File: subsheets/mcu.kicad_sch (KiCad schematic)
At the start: 4 parts

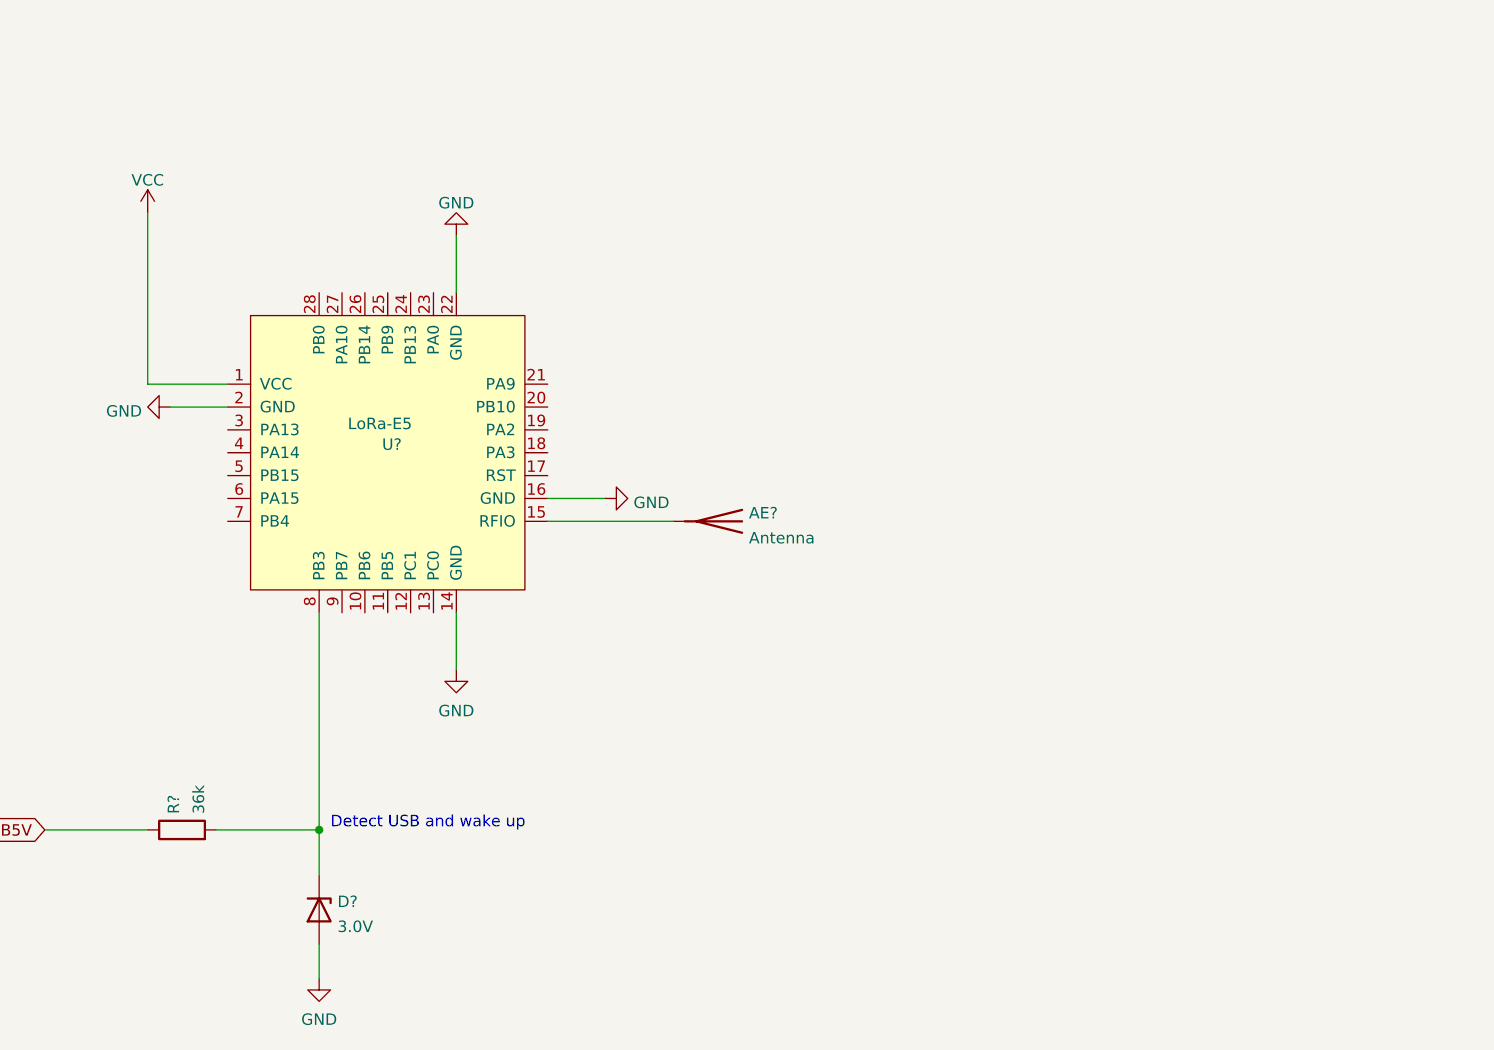
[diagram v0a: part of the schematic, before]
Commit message: Created Sensor Library
- Added Bosch BME688, SPS30, ZMOD symbols to MCU schematic
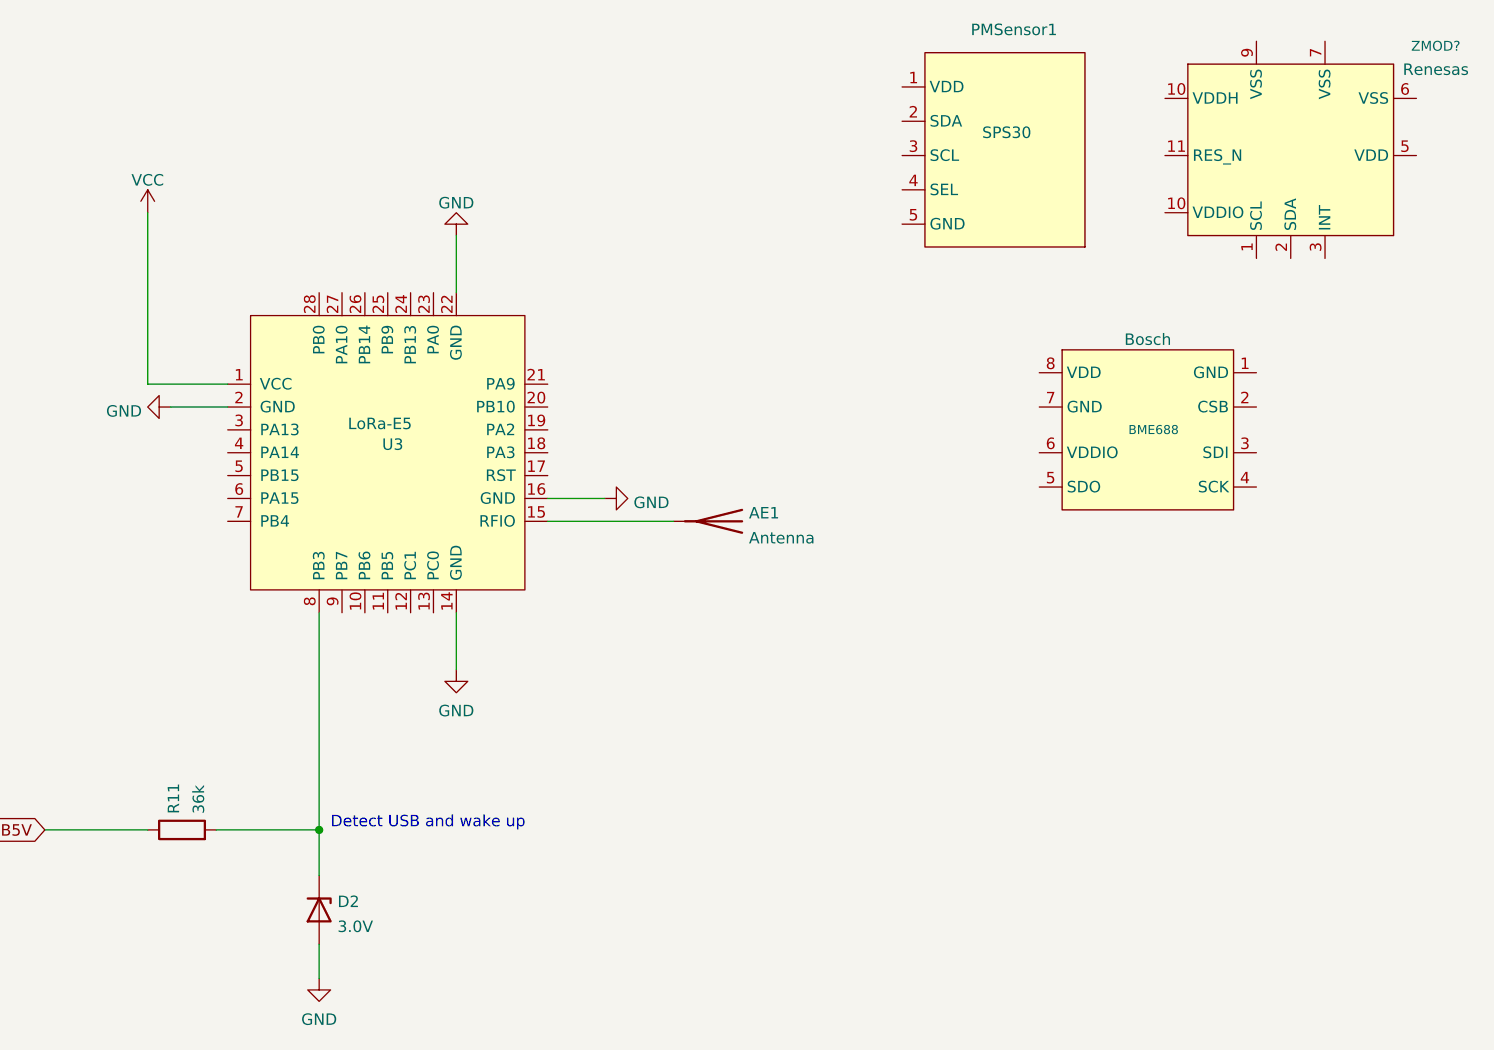
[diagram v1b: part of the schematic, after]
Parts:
- added BME688: Bosch, Package_LGA:LGA-12_2x2mm_P0.5mm, symbol sensors:Bosch
- added PMSensor1: SPS30, symbol sensors:SPS30
- added ZMOD?: Renesas, Package_LGA:LGA-12_2x2mm_P0.5mm, symbol sensors:Renesas
- gave numbers to parts that had none: 4
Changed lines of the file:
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@@
   (symbol (lib_id "power:GND") (at 120.65 71.12 270) (unit 1)
     (in_bom yes) (on_board yes) (fields_autoplaced)
-    (property "Reference" "#PWR?" (id 0) (at 114.3 71.12 0)
+    (property "Reference" "#PWR019" (id 0) (at 114.3 71.12 0)
       (effects (font (size 1.27 1.27)) hide)
     )
@@
   (symbol (lib_id "power:VCC") (at 118.11 49.53 0) (unit 1)
     (in_bom yes) (on_board yes) (fields_autoplaced)
-    (property "Reference" "#PWR?" (id 0) (at 118.11 53.34 0)
+    (property "Reference" "#PWR018" (id 0) (at 118.11 53.34 0)
       (effects (font (size 1.27 1.27)) hide)
     )
@@
   (symbol (lib_id "LoRa-E5:LoRa-E5") (at 144.78 76.2 0) (unit 1)
     (in_bom yes) (on_board yes)
-    (property "Reference" "U?" (id 0) (at 144.1451 75.2915 0)
+    (property "Reference" "U3" (id 0) (at 144.1451 75.2915 0)
       (effects (font (size 1.27 1.27)) (justify left))
     )
@@
     (pin "9")
   )
+  (symbol (lib_id "sensors:Renesas") (at 245.11 39.37 0) (unit 1)
+    (in_bom yes) (on_board yes) (fields_autoplaced)
+    (property "Reference" "ZMOD?" (id 0) (at 261.2313 31.0256 0)
+      (effects (font (size 1.1 1.1)))
+    )
+    (property "Value" "Renesas" (id 1) (at 261.2313 33.6318 0))
+    (property "Footprint" "Package_LGA:LGA-12_2x2mm_P0.5mm" (id 2) (at 245.11 39.37 0)
+      (effects (font (size 1.27 1.27)) hide)
+    )
+    (property "Datasheet" "" (id 3) (at 245.11 39.37 0)
+      (effects (font (size 1.27 1.27)) hide)
+    )
+    (pin "1")
+    (pin "10")
+    (pin "10")
+    (pin "11")
+    (pin "2")
+    (pin "3")
+    (pin "5")
+    (pin "6")
+    (pin "7")
+    (pin "8")
+    (pin "9")
+    (pin "n.c")
+  )
   (symbol (lib_id "Device:R") (at 121.92 118.11 90) (unit 1)
     (in_bom yes) (on_board yes) (fields_autoplaced)
-    (property "Reference" "R?" (id 0) (at 121.0115 116.332 0)
+    (property "Reference" "R11" (id 0) (at 121.0115 116.332 0)
       (effects (font (size 1.27 1.27)) (justify left))
     )
@@
   (symbol (lib_id "power:GND") (at 152.4 100.33 0) (unit 1)
     (in_bom yes) (on_board yes) (fields_autoplaced)
-    (property "Reference" "#PWR?" (id 0) (at 152.4 106.68 0)
+    (property "Reference" "#PWR022" (id 0) (at 152.4 106.68 0)
       (effects (font (size 1.27 1.27)) hide)
     )
@@
   (symbol (lib_id "power:GND") (at 137.16 134.62 0) (unit 1)
     (in_bom yes) (on_board yes) (fields_autoplaced)
-    (property "Reference" "#PWR?" (id 0) (at 137.16 140.97 0)
+    (property "Reference" "#PWR020" (id 0) (at 137.16 140.97 0)
       (effects (font (size 1.27 1.27)) hide)
     )
@@
     (pin "1")
   )
+  (symbol (lib_id "sensors:SPS30") (at 213.36 43.18 0) (unit 1)
+    (in_bom yes) (on_board yes)
+    (property "Reference" "PMSensor1" (id 0) (at 209.55 29.21 0)
+      (effects (font (size 1.27 1.27)) (justify left))
+    )
+    (property "Value" "SPS30" (id 1) (at 210.82 40.64 0)
+      (effects (font (size 1.27 1.27)) (justify left))
+    )
+    (property "Footprint" "" (id 2) (at 213.36 43.18 0)
+      (effects (font (size 1.27 1.27)) hide)
+    )
+    (property "Datasheet" "" (id 3) (at 213.36 43.18 0)
+      (effects (font (size 1.27 1.27)) hide)
+    )
+    (pin "1")
+    (pin "2")
+    (pin "3")
+    (pin "4")
+    (pin "5")
+  )
   (symbol (lib_id "power:GND") (at 168.91 81.28 90) (unit 1)
     (in_bom yes) (on_board yes) (fields_autoplaced)
-    (property "Reference" "#PWR?" (id 0) (at 175.26 81.28 0)
+    (property "Reference" "#PWR023" (id 0) (at 175.26 81.28 0)
       (effects (font (size 1.27 1.27)) hide)
     )
@@
   (symbol (lib_id "power:GND") (at 152.4 52.07 180) (unit 1)
     (in_bom yes) (on_board yes) (fields_autoplaced)
-    (property "Reference" "#PWR?" (id 0) (at 152.4 45.72 0)
+    (property "Reference" "#PWR021" (id 0) (at 152.4 45.72 0)
       (effects (font (size 1.27 1.27)) hide)
     )
@@
   (symbol (lib_id "Device:Antenna") (at 181.61 83.82 270) (unit 1)
     (in_bom yes) (on_board yes) (fields_autoplaced)
-    (property "Reference" "AE?" (id 0) (at 184.9119 82.9115 90)
+    (property "Reference" "AE1" (id 0) (at 184.9119 82.9115 90)
       (effects (font (size 1.27 1.27)) (justify left))
     )
@@
   (symbol (lib_id "Device:D_Zener") (at 137.16 127 270) (unit 1)
     (in_bom yes) (on_board yes) (fields_autoplaced)
-    (property "Reference" "D?" (id 0) (at 139.192 126.0915 90)
+    (property "Reference" "D2" (id 0) (at 139.192 126.0915 90)
       (effects (font (size 1.27 1.27)) (justify left))
     )
@@
     (pin "2")
   )
+  (symbol (lib_id "sensors:Bosch") (at 228.6 73.66 0) (unit 1)
+    (in_bom yes) (on_board yes)
+    (property "Reference" "BME688" (id 0) (at 229.87 73.66 0)
+      (effects (font (size 1 1)))
+    )
+    (property "Value" "Bosch" (id 1) (at 229.235 63.6293 0))
+    (property "Footprint" "Package_LGA:LGA-12_2x2mm_P0.5mm" (id 2) (at 228.6 73.66 0)
+      (effects (font (size 1.27 1.27)) hide)
+    )
+    (property "Datasheet" "" (id 3) (at 228.6 73.66 0)
+      (effects (font (size 1.27 1.27)) hide)
+    )
+    (pin "1")
+    (pin "2")
+    (pin "3")
+    (pin "4")
+    (pin "5")
+    (pin "6")
+    (pin "7")
+    (pin "8")
+  )
 )

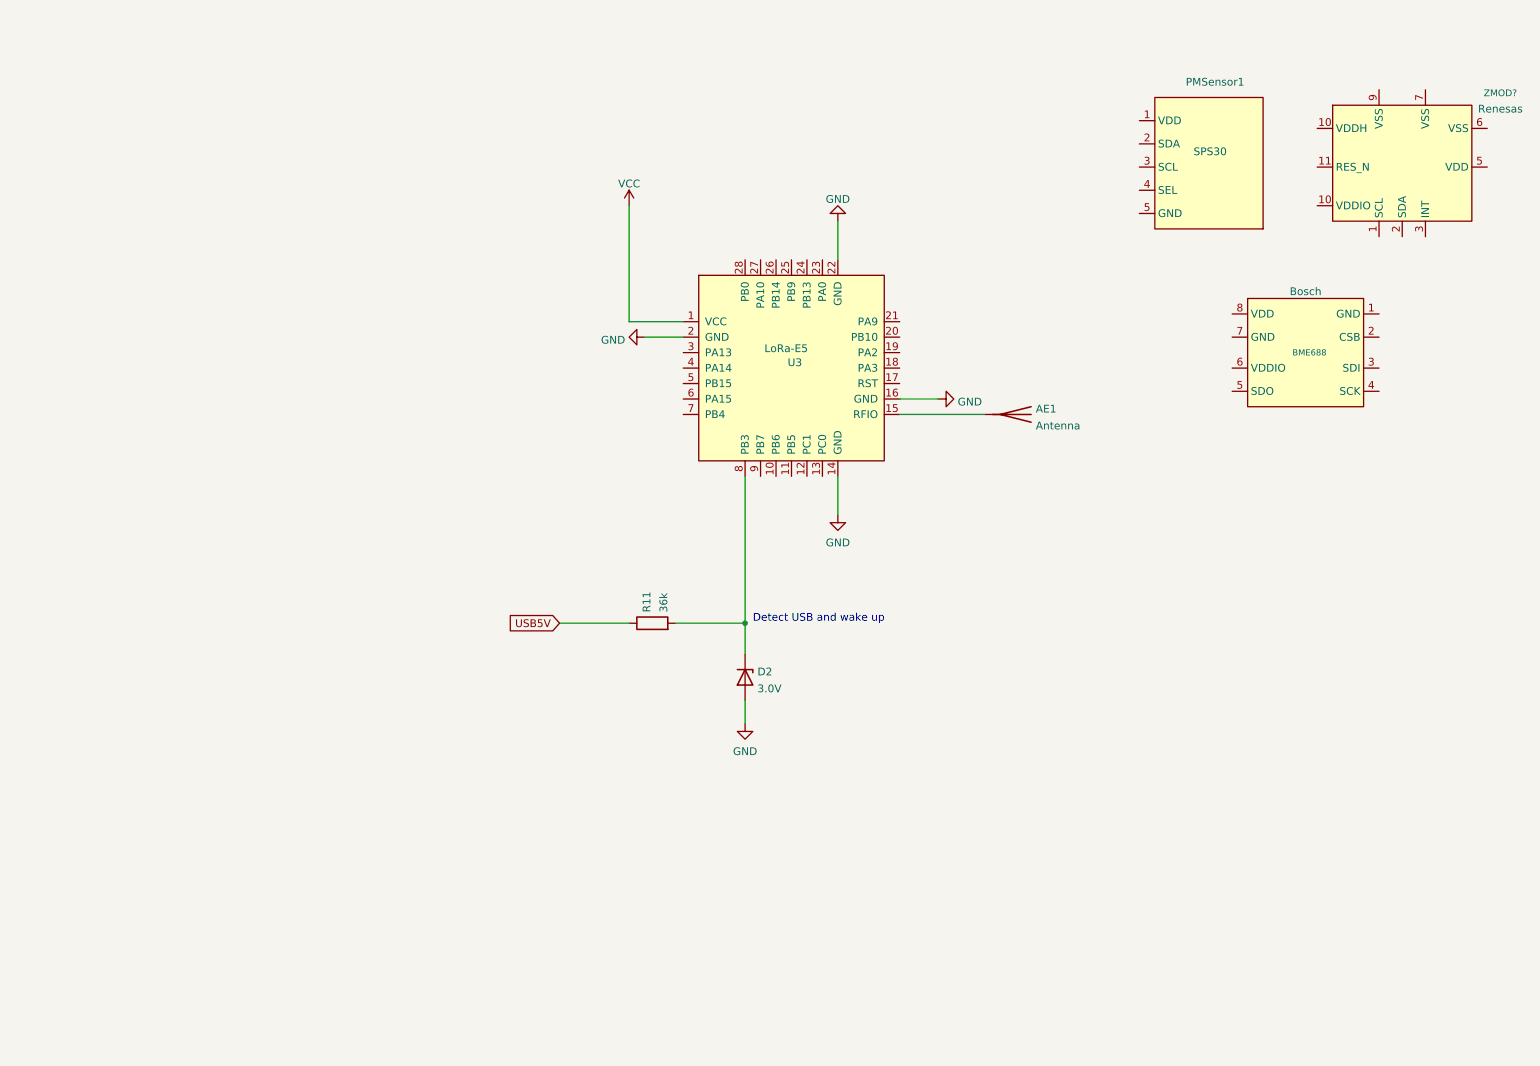
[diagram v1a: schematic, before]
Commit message: Connected ZMOD and Bosch Sensors
-
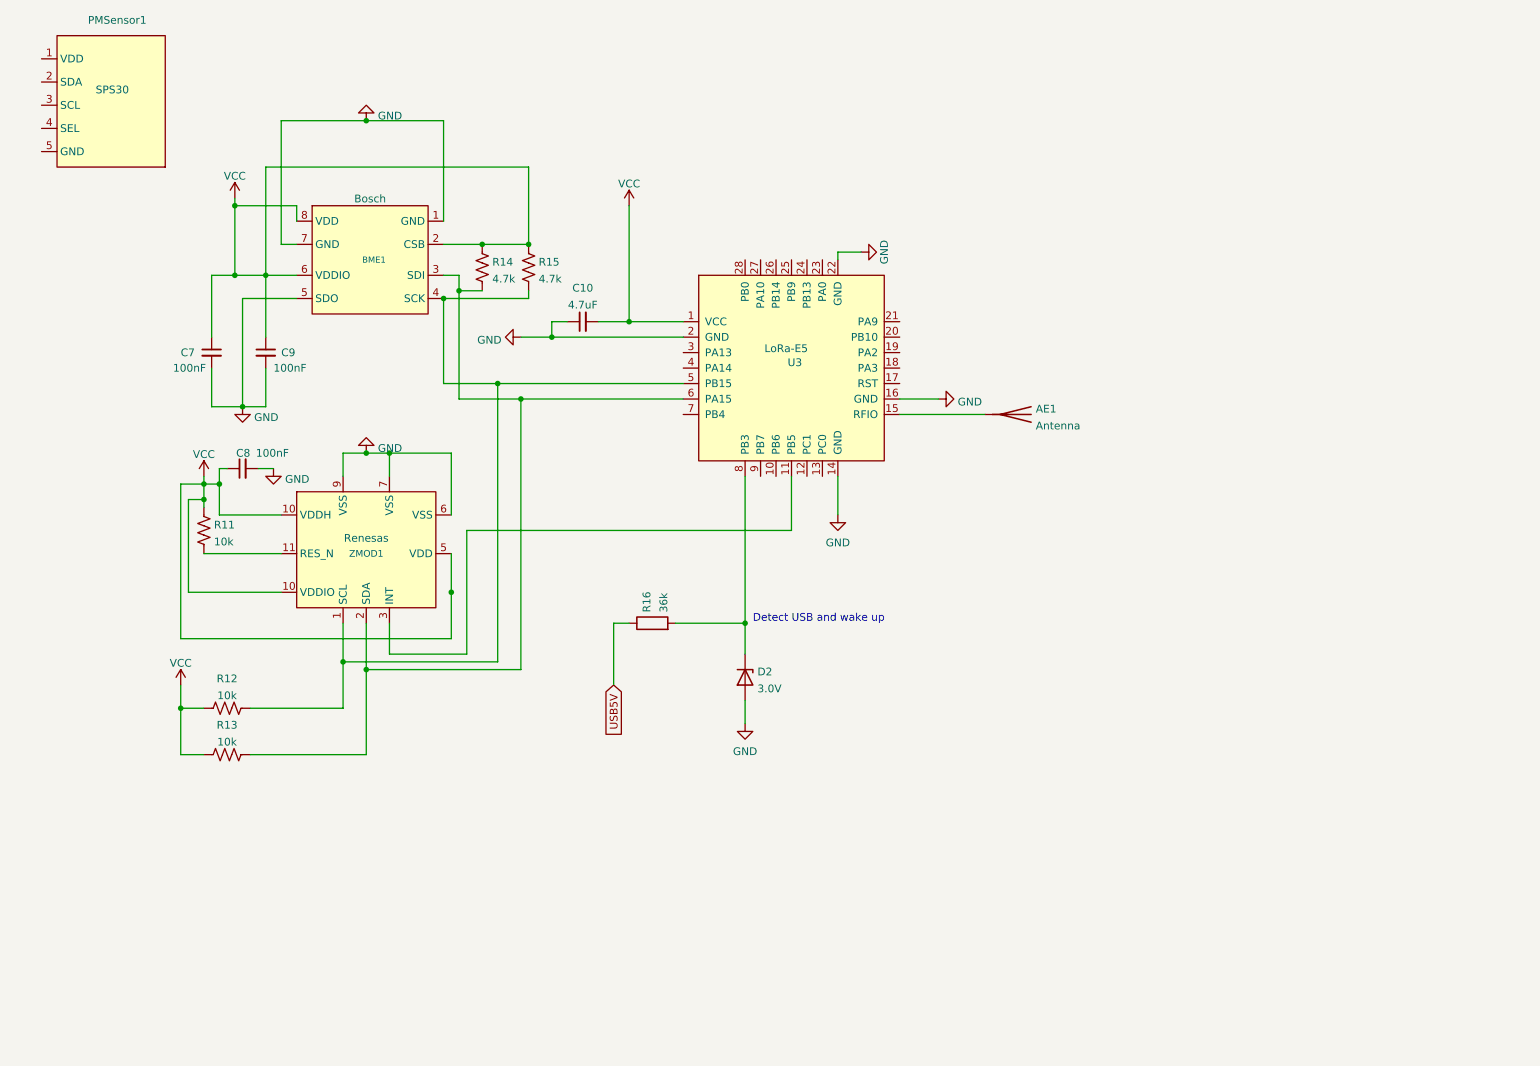
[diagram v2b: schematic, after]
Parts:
- added C10: 4.7uF, symbol Device:C_Small
- added C7, C8, C9: 100nF, symbol Device:C_Small
- added R11, R12, R13: 10k, symbol Device:R_US
- added R14, R15: 4.7k, symbol Device:R_US
- gave numbers to parts that had none: 1
- renumbered BME688 to BME1, R11 to R16
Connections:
- net GND: now also BME1.1 (GND), BME1.5 (SDO), BME1.7 (GND), ZMOD1.6 (VSS), ZMOD1.7 (VSS), ZMOD1.9 (VSS), C10.1, C7.2, C8.2, C9.2
- net VCC: now also BME1.2 (CSB), BME1.6 (VDDIO), BME1.8 (VDD), ZMOD1.10 (VDDIO), ZMOD1.5 (VDD), ZMOD1.n.c (4), C10.2, C7.1, C8.1, C9.1, R11.1, R12.1, R13.1, R14.1, R15.1
- net at U3.11 (PB5): now also ZMOD1.3 (INT)
- net at U3.5 (PB15): now also BME1.4 (SCK), ZMOD1.1 (SCL), R12.2, R15.2
- net at U3.6 (PA15): now also BME1.3 (SDI), ZMOD1.2 (SDA), R13.2, R14.2
- net at ZMOD1.11 (RES_N): now also R11.2
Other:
- moved on the sheet: BME1, PMSensor1, ZMOD1
